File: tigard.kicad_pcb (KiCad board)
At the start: 2 copper layers, 89 parts, among them J1 USB_C_Receptacle_USB2.0, J2 JTAG, J3 UART, J4 SPI, J5 CORTEX, J6 LA, J7 I2C, Q1 BSH103, SW1 TARGET, SW2 MODE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

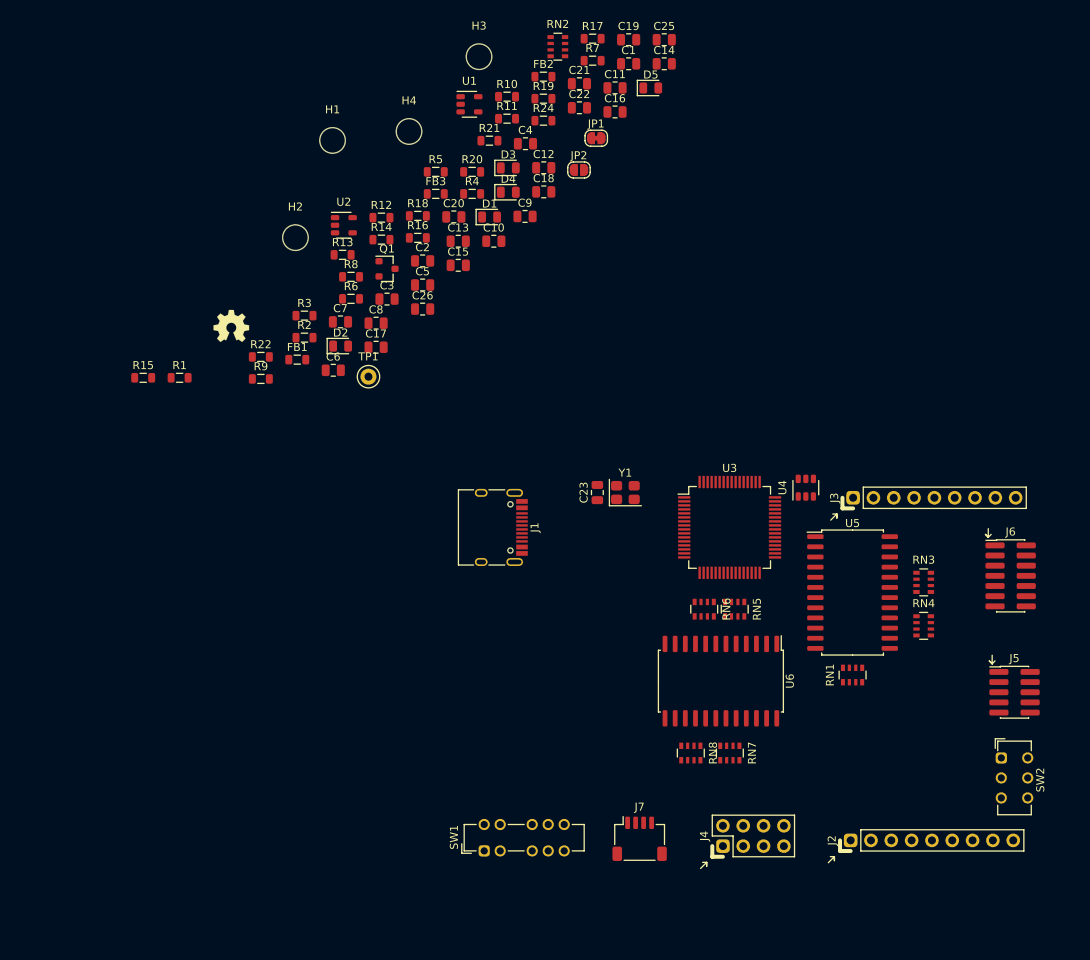
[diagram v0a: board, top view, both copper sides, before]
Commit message: tomk-tigard-lts: progress commit - board outline
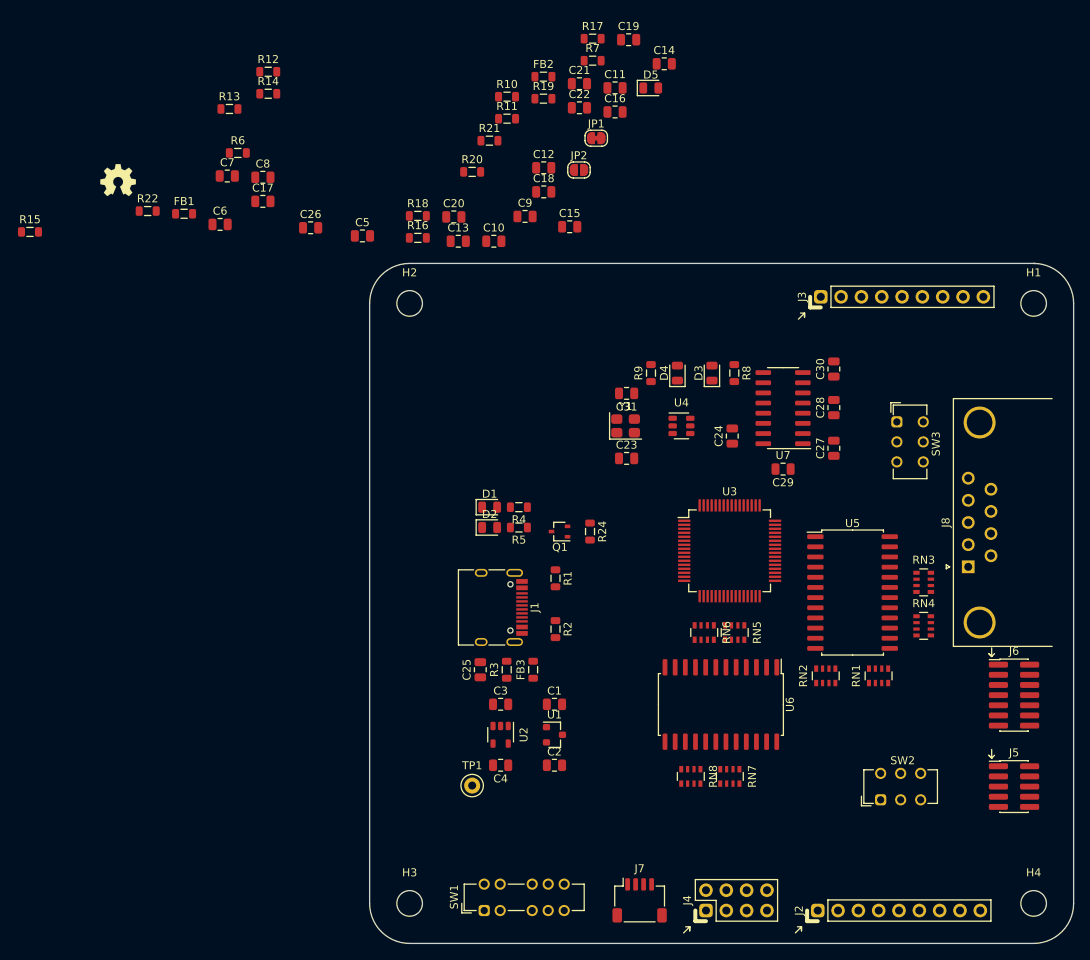
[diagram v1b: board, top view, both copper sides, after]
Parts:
- added C24: 100n, Capacitor_SMD:C_0805_2012Metric, F.Cu at (100.3, 68.6)
- added C27: 100n, Capacitor_SMD:C_0805_2012Metric, F.Cu at (113.0, 70.1)
- added C28: 100n, Capacitor_SMD:C_0805_2012Metric, F.Cu at (113.0, 65.0)
- added C29: 100n, Capacitor_SMD:C_0805_2012Metric, F.Cu at (106.7, 72.7)
- added C30: 100n, Capacitor_SMD:C_0805_2012Metric, F.Cu at (113.0, 60.2)
- added C31: 30pF, Capacitor_SMD:C_0805_2012Metric, F.Cu at (87.1, 63.2)
- added J8: DB9_Male_MountingHoles, Connector_Dsub:DSUB-9_Male_Horizontal_P2.77x2.84mm_EdgePinOffset7.70mm_Housed_MountingHolesOffset9.12mm, F.Cu at (129.8, 84.9)
- added SW3: RXSRC, tigard:SW_CuK_JS202011CQN_DPDT_Straight, F.Cu at (120.9, 66.8)
- added U7: MAX202, Package_SO:SOIC-16_3.9x9.9mm_P1.27mm, F.Cu at (106.7, 65.1)
- Q1: value BSH103 -> NTS4409NT1G; footprint tigard:SOT-23_RoundRect -> Package_TO_SOT_SMD:SOT-323_SC-70
- U1: value AP7365-18 -> AP7313-18SAG-7; footprint tigard:SOT-23-5_RoundRect -> tigard:SOT-23_RoundRect
- U2: value AP7365-33 -> MIC5205-3.3YM5
- moved H4 124.1 mm to (138.0, 127.0)
- moved H3 106.2 mm to (60.0, 127.0)
- moved H1 90.0 mm to (138.0, 52.0)
- moved RN2 85.5 mm to (112.0, 98.6), turned to 90 degrees
- moved C25 82.0 mm to (68.8, 97.8), turned to 90 degrees
- moved C1 80.6 mm to (78.1, 102.1)
- moved U1 79.5 mm to (78.1, 105.9)
- moved C4 77.8 mm to (71.4, 109.7), turned to 180 degrees
- moved U2 66.6 mm to (71.4, 105.9), turned to -90 degrees
- moved C2 65.2 mm to (78.1, 109.7)
- moved FB3 60.7 mm to (75.4, 97.8), turned to 90 degrees
- moved R1 53.3 mm to (78.2, 86.4), turned to -90 degrees
- moved TP1 52.7 mm to (67.8, 112.3)
- moved C3 52.6 mm to (71.4, 102.1)
- moved R24 51.7 mm to (82.5, 80.5), turned to -90 degrees
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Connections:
- net /xPB2 renamed /DI
- net /xPB7 renamed /ICE_CDONE
- RN6 pad 4: /AD1 -> Net-(RN6-Pad4)
- U1 pad 2: GND -> +1V8
- U1 pad 3: +5V -> unconnected-(U1-Pad3)
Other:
- board outline added: 88 x 85 mm

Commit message: tigard-lts: progress commit
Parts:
- added LOGO2: Logo_Open_Hardware_Small, tigard:Tigard_Logo, F.Cu at (72.1, 91.8)
- added R23: 0R, Inductor_SMD:L_0805_2012Metric, F.Cu at (125.2, 78.1)
- JP1, JP2: moved to B.Cu
- moved R17 102.4 mm to (75.3, 121.0), turned to 90 degrees
- moved JP2 102.1 mm to (132.4, 123.6)
- moved JP1 95.1 mm to (82.3, 126.5), turned to -90 degrees
- moved R16 94.3 mm to (128.7, 109.5)
- moved R21 93.9 mm to (98.3, 121.2)
- moved R20 92.8 mm to (103.6, 121.2), turned to 180 degrees
- moved R22 87.8 mm to (107.2, 76.8)
- moved D5 87.7 mm to (57.6, 106.5)
- moved C22 87.1 mm to (105.9, 111.1), turned to -90 degrees
- moved R10 83.3 mm to (61.9, 108.9), turned to 180 degrees
- moved R11 78.3 mm to (61.9, 106.5)
- moved R19 77.7 mm to (108.2, 97.4), turned to 90 degrees
- moved C7 71.8 mm to (89.4, 85.5), turned to -90 degrees
- moved R7 70.7 mm to (91.2, 91.8), turned to 90 degrees
- moved C8 70.3 mm to (91.8, 85.5), turned to -90 degrees
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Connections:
- RN1 pad 5: /BD4 -> /BD5
- RN1 pad 6: /BD3 -> /BD4
- RN1 pad 7: /BD1 -> /BD3
- RN1 pad 8: /BD0 -> /BD1
- RN2 pad 5: /AD0 -> /BD0
- RN2 pad 6: /AD2 -> /AD4
- RN2 pad 7: /AD4 -> /AD2
- RN2 pad 8: /BD5 -> /AD0
- RN3 pad 5: /xPB4 -> /COPI
- RN3 pad 7: /COPI -> /xPB4
- RN3 pad 8: /CLK -> /xPB5
- RN4 pad 8: /xPB5 -> /CLK
- U5 pad 3: /BD0 -> /BD5
- U5 pad 4: /BD1 -> /BD4
- U5 pad 6: /BD4 -> /BD1
- U5 pad 7: /BD5 -> /BD0
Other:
- outline, holes or cut-outs redrawn
- board text added: "LTS"

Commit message: tomk-tigard-lts: progress commit
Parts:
- moved R23 37.3 mm to (91.9, 95.0), turned to 180 degrees
- moved RN1 1.27 mm to (117.3, 98.6)
- moved RN2 1.27 mm to (113.3, 98.5)
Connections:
- C23 pad 1: Net-(C23-Pad1) -> Net-(U3-Pad3)
- C31 pad 1: Net-(C31-Pad1) -> Net-(U3-Pad2)
- U3 pad 2: Net-(C23-Pad1) -> Net-(U3-Pad2)
- U3 pad 3: Net-(C31-Pad1) -> Net-(U3-Pad3)
- Y1 pad 1: Net-(C23-Pad1) -> Net-(U3-Pad3)
- Y1 pad 3: Net-(C31-Pad1) -> Net-(U3-Pad2)
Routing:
- net +3V3: track 0.00 -> 40.3 mm
- net VREF: track 0.00 -> 37.5 mm
- net /USB_DN: track 0.00 -> 37.5 mm
- net /USB_DP: track 0.00 -> 36.5 mm
- net /BD5: track 0.00 -> 29.9 mm
- net /AD4: track 0.00 -> 24.8 mm, vias 0 -> 2
- net /AD2: track 0.00 -> 23.9 mm, vias 0 -> 2
- net Net-(C25-Pad2): track 0.00 -> 23.4 mm
- net VREG: track 0.00 -> 23.2 mm
- net /BD4: track 0.00 -> 22.3 mm
- net Net-(U3-Pad2): track 0.00 -> 20.9 mm
- net /BD3: track 0.00 -> 20.8 mm
- net /BD1: track 0.00 -> 19.4 mm
- net Net-(U3-Pad3): track 0.00 -> 19.2 mm
- net /BD0: track 0.00 -> 18.1 mm
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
